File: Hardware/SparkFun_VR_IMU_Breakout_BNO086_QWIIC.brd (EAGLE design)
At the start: 30.5 x 25.4 mm, 99 parts, among them J2 SMD, J3 PTH, J4 SMD, J6 SPI, U2 BNO086, Y1 32.768kHz

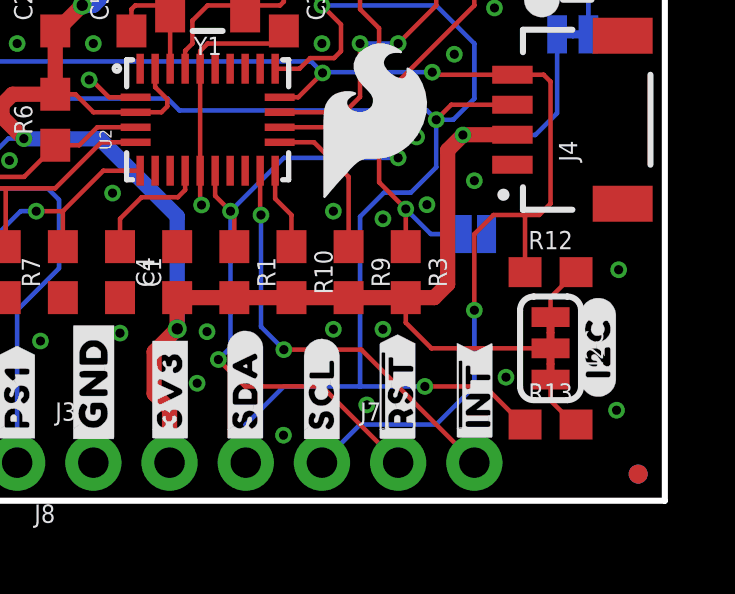
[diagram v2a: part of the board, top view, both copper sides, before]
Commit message: line in sch to dash, address options in silk
-corrected a line in SCH to match others as dashed
-Added bottom silk to show address options
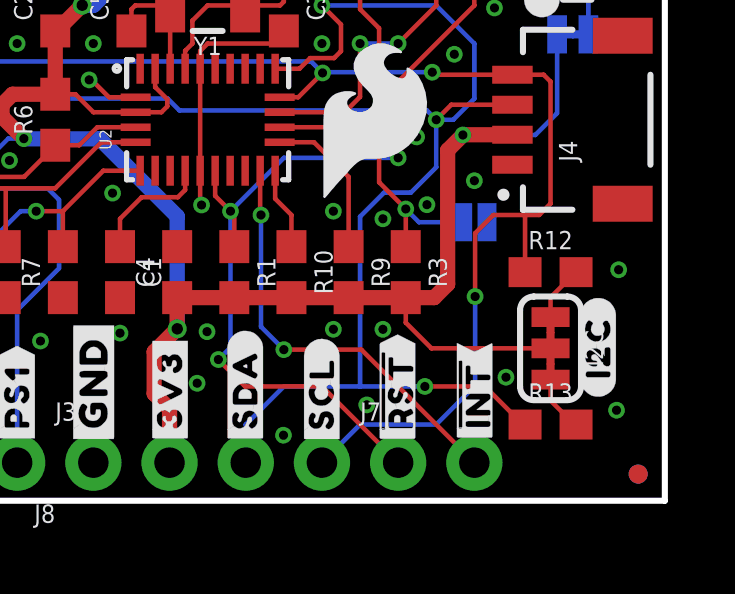
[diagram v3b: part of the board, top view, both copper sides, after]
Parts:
- added U$28: (no value), output:OPEN#0X4B0
- added U$58: (no value), output:CLOSED#0X4A0
- added U$61: (no value), output:DEFAULT0
- moved U$52 1.31 mm to (23.3, 13.4)
- moved LOGO5 1.29 mm to (14.6, 8.78)
- moved U$30 0.46 mm to (26.9, 9.38)
- moved ADR 0.39 mm to (24.1, 9.28)
- moved U$54 0.23 mm to (12.0, 13.4)
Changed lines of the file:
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@@
 <wire x1="1.8161" y1="17.139921875" x2="2.6898625" y2="17.139921875" width="0.1778" layer="21"/>
 <wire x1="1.8161" y1="17.139921875" x2="2.6898625" y2="17.139921875" width="0.1778" layer="22"/>
+<wire x1="21.445225" y1="6.789415625" x2="21.49601875" y2="5.788659375" width="0.1524" layer="22" curve="-126.475581"/>
+<wire x1="16.65985625" y1="5.803903125" x2="16.687796875" y2="6.77671875" width="0.1524" layer="22" curve="-126.475581"/>
 </plain>
 <attributes>
@@
 <attribute name="VALUE" x="15.367" y="7.62" size="0.6096" layer="27" font="vector" ratio="20" rot="R270" align="top-center"/>
 </element>
-<element name="ADR" library="SparkFun-Jumpers" package="SMT-JUMPER_2_NO_SILK" package3d_urn="urn:adsk.eagle:package:39279/1" value="" x="24.13" y="8.89" smashed="yes" rot="MR0">
-<attribute name="NAME" x="25.038" y="10.16" size="0.4064" layer="26" rot="MR0"/>
-<attribute name="VALUE" x="25.038" y="7.239" size="0.4064" layer="28" rot="MR0"/>
+<element name="ADR" library="SparkFun-Jumpers" package="SMT-JUMPER_2_NO_SILK" package3d_urn="urn:adsk.eagle:package:39279/1" value="" x="24.145240625" y="9.2837" smashed="yes" rot="MR0">
+<attribute name="NAME" x="25.053240625" y="10.5537" size="0.4064" layer="26" rot="MR0"/>
+<attribute name="VALUE" x="25.053240625" y="7.6327" size="0.4064" layer="28" rot="MR0"/>
 </element>
 <element name="R3" library="SparkFun-Resistors" package="0603" value="10k" x="21.844" y="7.62" smashed="yes" rot="R270">
@@
 </element>
 <element name="LOGO4" library="SparkFun-Aesthetics" package="SFE_LOGO_FLAME_.2" value="SFE_LOGO_FLAME.2_INCH" x="20.817840625" y="12.6492" smashed="yes"/>
-<element name="LOGO5" library="SparkFun-Aesthetics" package="SFE_LOGO_NAME_FLAME_.1" value="SFE_LOGO_NAME_FLAME.1_INCH" x="15.181578125" y="7.642859375" smashed="yes" rot="MR0"/>
+<element name="LOGO5" library="SparkFun-Aesthetics" package="SFE_LOGO_NAME_FLAME_.1" value="SFE_LOGO_NAME_FLAME.1_INCH" x="14.5821375" y="8.780778125" smashed="yes" rot="MR0"/>
 <element name="PWR" library="SparkFun-LED" package="LED-0603" value="RED" x="27.559" y="18.288" smashed="yes" rot="R270">
 <attribute name="NAME" x="28.194" y="18.288" size="0.6096" layer="25" font="vector" ratio="20" rot="R270" align="bottom-center"/>
@@
 <element name="U$25" library="output" package="X878" value="" x="4.358640625" y="17.12721875" smashed="yes" rot="MR0"/>
 <element name="U$29" library="SparkFun-Aesthetics" package="QWIIC_4MM" value="" x="1.089659375" y="3.533140625" smashed="yes" rot="R90"/>
-<element name="U$52" library="SparkFun-Aesthetics" package="QWIIC_6MM" value="" x="24.6126" y="13.07591875" smashed="yes" rot="MR0"/>
-<element name="U$54" library="output" package="BNO086_IMU881" value="" x="12.00658125" y="13.1597375" smashed="yes" rot="MR0"/>
+<element name="U$52" library="SparkFun-Aesthetics" package="QWIIC_6MM" value="" x="23.327359375" y="13.352778125" smashed="yes" rot="MR0"/>
+<element name="U$54" library="output" package="BNO086_IMU881" value="" x="12.00658125" y="13.385796875" smashed="yes" rot="MR0"/>
 <element name="U$44" library="output" package="UART881" value="" x="25.8064" y="18.01368125" smashed="yes" rot="MR0"/>
 <element name="U$39" library="output" package="#3V3#882" value="" x="8.88238125" y="21.727159375" smashed="yes" rot="MR90"/>
@@
 <element name="U$21" library="output" package="RXI891" value="" x="16.499840625" y="16.537940625" smashed="yes" rot="MR90"/>
 <element name="U$22" library="output" package="TXO892" value="" x="19.052540625" y="16.220440625" smashed="yes" rot="MR90"/>
-<element name="U$30" library="output" package="#ADR#894" value="" x="26.84271875" y="8.917940625" smashed="yes" rot="MR0"/>
+<element name="U$30" library="output" package="#ADR#894" value="" x="26.890978125" y="9.375140625" smashed="yes" rot="MR0"/>
 <element name="U$35" library="output" package="#PS1#895" value="" x="3.91668125" y="8.887459375" smashed="yes" rot="MR0"/>
 <element name="U$57" library="output" package="#PS0#895" value="" x="3.794759375" y="6.31698125" smashed="yes" rot="MR0"/>
@@
 </element>
 <element name="U$26" library="output" package="#LED#0" value="" x="24.81071875" y="15.504159375" smashed="yes" rot="MR0"/>
+<element name="U$28" library="output" package="OPEN#0X4B0" value="" x="25.242521875" y="6.278878125" smashed="yes" rot="MR0"/>
+<element name="U$58" library="output" package="CLOSED#0X4A0" value="" x="25.63368125" y="7.5438" smashed="yes" rot="MR0"/>
+<element name="U$61" library="output" package="DEFAULT0" value="" x="19.0601625" y="6.31698125" smashed="yes" rot="MR0"/>
 </elements>
 <signals>
@@
 <wire x1="16.51" y1="24.13" x2="20.32" y2="20.32" width="0.1524" layer="1"/>
 <wire x1="20.32" y1="20.32" x2="20.32" y2="16.383" width="0.1524" layer="1"/>
-<wire x1="23.7236" y1="8.89" x2="22.679659375" y2="8.89" width="0.1524" layer="16"/>
-<wire x1="22.679659375" y1="8.89" x2="21.844" y2="9.725659375" width="0.1524" layer="16"/>
+<wire x1="23.738840625" y1="9.2837" x2="22.285959375" y2="9.2837" width="0.1524" layer="16"/>
+<wire x1="22.285959375" y1="9.2837" x2="21.844" y2="9.725659375" width="0.1524" layer="16"/>
 </signal>
 <signal name="!BOOT">
@@
 <wire x1="19.05" y1="1.27" x2="20.32" y2="2.54" width="0.1524" layer="16"/>
 <wire x1="20.32" y1="2.54" x2="22.86" y2="2.54" width="0.1524" layer="16"/>
-<wire x1="22.86" y1="2.54" x2="24.13" y2="3.81" width="0.1524" layer="16"/>
-<wire x1="24.13" y1="3.81" x2="24.13" y2="6.35" width="0.1524" layer="16"/>
-<via x="24.13" y="6.35" extent="1-16" drill="0.3048"/>
+<wire x1="22.86" y1="2.54" x2="24.1554" y2="3.8354" width="0.1524" layer="16"/>
+<wire x1="24.1554" y1="3.8354" x2="24.1554" y2="6.8072" width="0.1524" layer="16"/>
+<via x="24.1554" y="6.8072" extent="1-16" drill="0.3048"/>
 <wire x1="15.24" y1="20.32" x2="7.62" y2="20.32" width="0.1524" layer="16"/>
 <wire x1="7.62" y1="20.32" x2="6.35" y2="19.05" width="0.1524" layer="16"/>
@@
 <wire x1="25.82" y1="7.62" x2="25.82" y2="9.486" width="0.1524" layer="1"/>
 <wire x1="25.82" y1="9.486" x2="25.781" y2="9.525" width="0.1524" layer="1"/>
-<wire x1="24.13" y1="6.35" x2="24.13" y2="8.89" width="0.1524" layer="1"/>
-<wire x1="24.13" y1="8.89" x2="24.765" y2="9.525" width="0.1524" layer="1"/>
+<wire x1="24.1554" y1="6.8072" x2="24.1554" y2="8.9154" width="0.1524" layer="1"/>
+<wire x1="24.1554" y1="8.9154" x2="24.765" y2="9.525" width="0.1524" layer="1"/>
 <contactref element="J4" pad="4"/>
 <contactref element="J2" pad="4"/>
